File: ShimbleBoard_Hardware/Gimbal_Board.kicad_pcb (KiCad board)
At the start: 2 copper layers, 57 parts, among them Q1 2N3904, Q2 2N3904, Q3 2N3904, Q4 2N3904, Q5 2N3904, Q6 2N3904, Q7 2N3904, Q8 2N3904, U1 TM4C129E_Launchpad, U2 OKI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

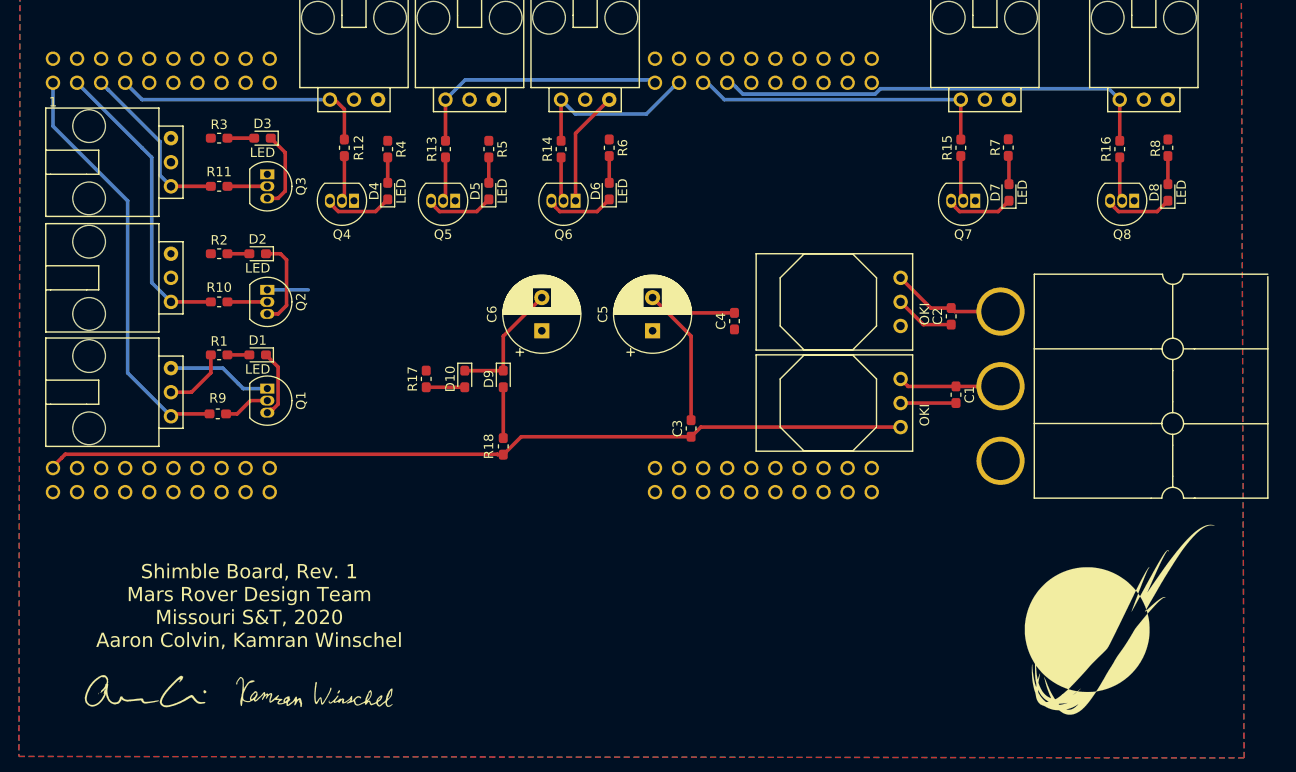
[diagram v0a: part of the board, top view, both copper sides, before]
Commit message: BJT changes
BJT changed to surface mount
Minor re-wiring
Ground & +5VA plains changed to solid
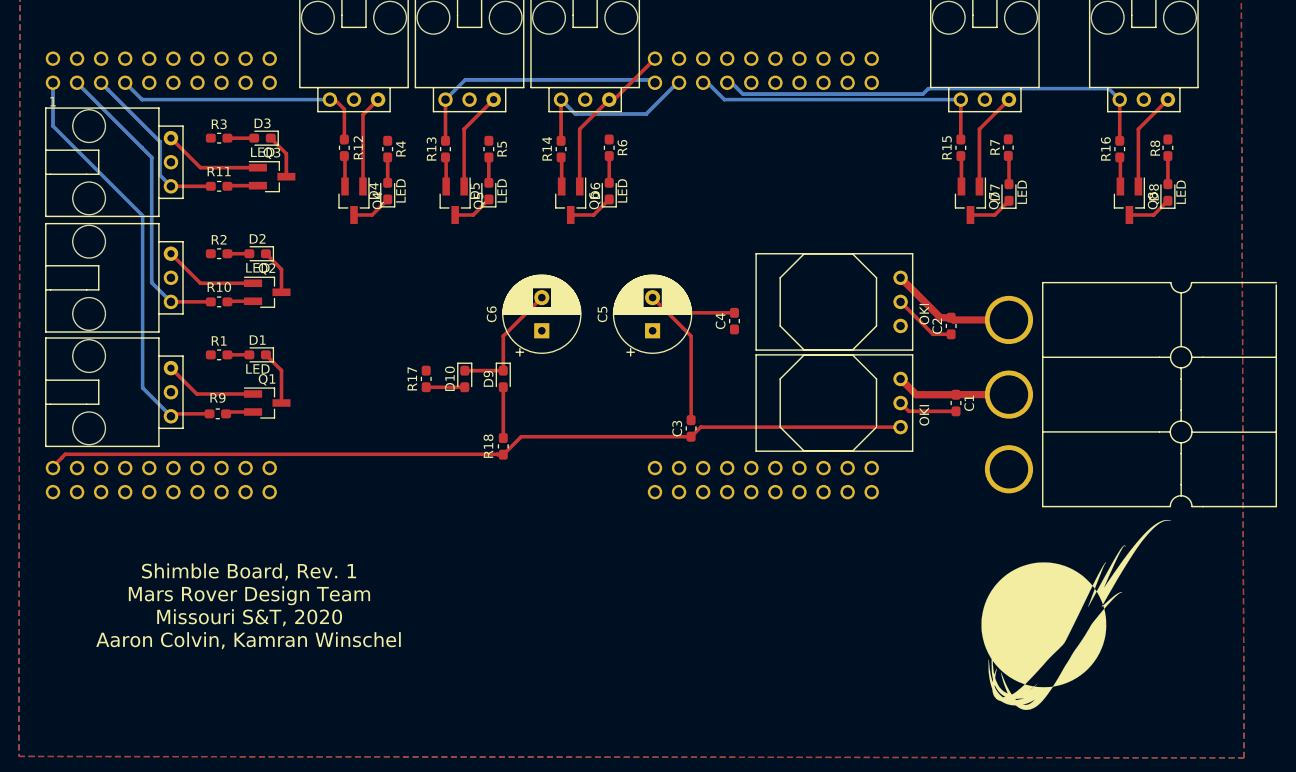
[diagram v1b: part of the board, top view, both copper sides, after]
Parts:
- removed the G*** at (97.0, 127.5)
- removed the G*** at (79.2, 127.5)
- Q1, Q2, Q3, Q4, Q5, Q6, Q7, Q8: footprint Package_TO_SOT_THT:TO-92_Inline -> Package_TO_SOT_SMD:SOT-23_Handsoldering
- moved G*** 4.60 mm to (177.3, 119.4)
- moved Q1 1.52 mm to (91.9, 97.0), turned to 0 degrees
- moved Conn9 1.26 mm to (173.7, 84.3)
- moved C2 1.02 mm to (164.1, 88.9)
- moved C1 0.88 mm to (164.6, 97.0)
- moved Q3 0.57 mm to (92.5, 73.2), turned to 0 degrees
- moved Q8 0.51 mm to (182.9, 75.7), turned to 270 degrees
- moved Q6 0.51 mm to (124.0, 75.7), turned to 270 degrees
- moved Q7 0.51 mm to (166.1, 75.7), turned to 270 degrees
- moved Q2 0.25 mm to (91.9, 85.3), turned to 0 degrees
- turned Q4 to 270 degrees
- turned Q5 to 270 degrees
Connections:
- U1 pad +5V: Net-(U1-Pad+5V) -> +5VL
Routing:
- net GND: track 74.8 -> 136.5 mm
- net +5VA: track 6.94 -> 0.00 mm
- net Net-(D2-Pad1): track 9.66 -> 4.74 mm
- net Net-(D3-Pad1): track 8.43 -> 4.74 mm
- net Net-(D5-Pad1): track 7.25 -> 4.24 mm
- net Net-(D4-Pad1): track 7.25 -> 4.24 mm
- net Net-(D7-Pad1): track 7.19 -> 4.69 mm
- net Net-(D6-Pad1): track 7.25 -> 4.74 mm
- net Net-(D8-Pad1): track 7.19 -> 4.69 mm
- net Net-(Q1-Pad2): track 5.28 -> 2.93 mm
- net Net-(Q7-Pad2): track 4.82 -> 3.24 mm
- net Net-(Q6-Pad2): track 4.68 -> 3.10 mm
- net Net-(Q5-Pad2): track 4.68 -> 3.10 mm
- net Net-(Q8-Pad2): track 4.68 -> 3.10 mm
- net Net-(Q4-Pad2): track 4.82 -> 3.24 mm
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
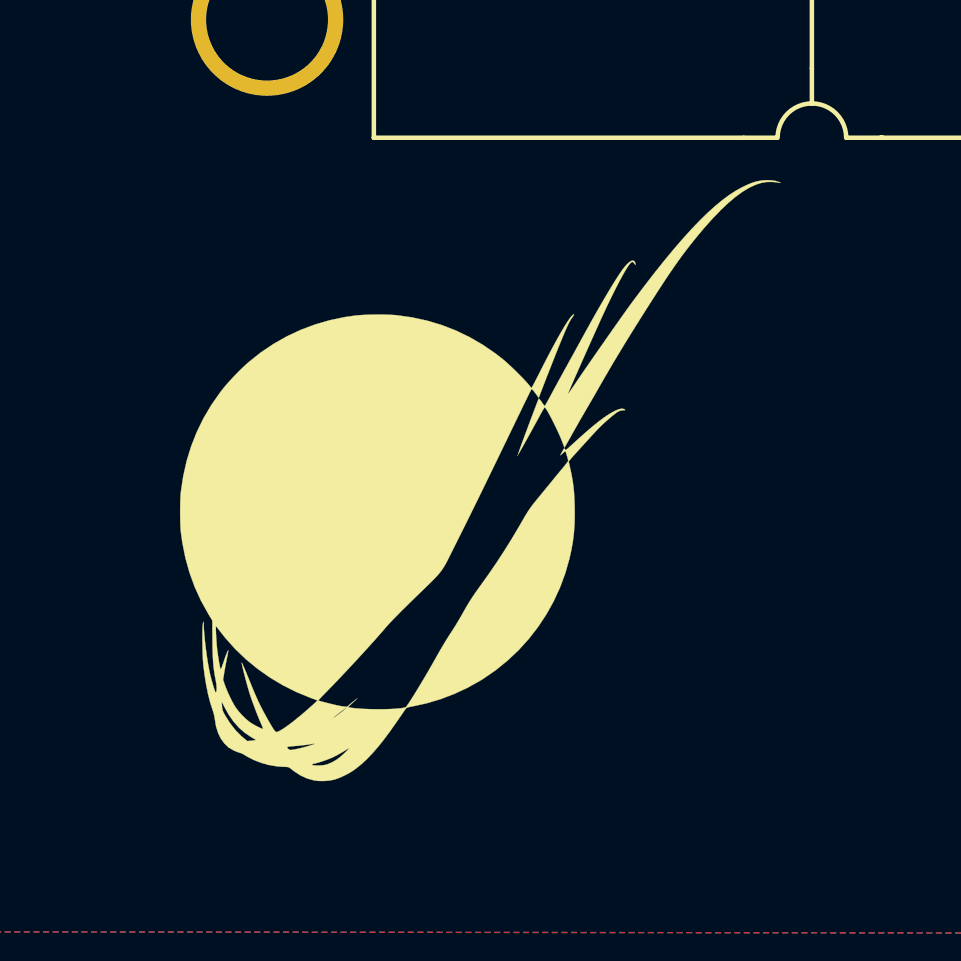
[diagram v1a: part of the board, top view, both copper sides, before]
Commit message: Resistor Changes
Resistors changed to 500 standard
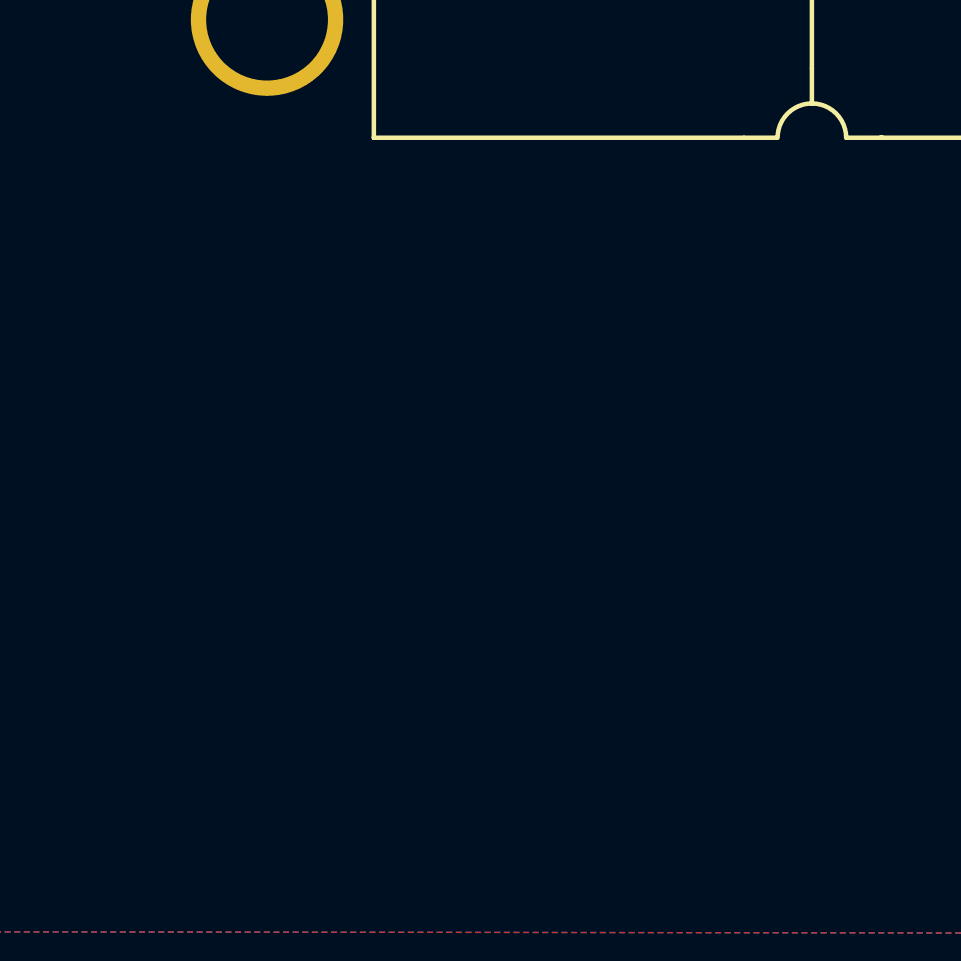
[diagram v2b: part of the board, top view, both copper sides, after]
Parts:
- removed G***: LOGO, MRDT_Silkscreens:0_MRDT_Logo_20mm
- R1, R10, R11, R12, R13, R14, R15, R16, R2, R3, R4, R5, R6, R7, R8, R9: value 100 -> 500
- R17, R18: value 1000 -> 500

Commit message: Major Overhaull
BJTs replaced by N-MOSFET
Buttons & switch added
PCB layout worked on (still not complete)
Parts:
- added D10: LED, Diode_SMD:D_0603_1608Metric_Pad1.05x0.95mm_HandSolder, F.Cu at (-66.5, 56.8)
- added D11: LED, Diode_SMD:D_0603_1608Metric_Pad1.05x0.95mm_HandSolder, F.Cu at (-56.9, 56.8)
- added D12: LED, Diode_SMD:D_0603_1608Metric_Pad1.05x0.95mm_HandSolder, F.Cu at (-47.2, 56.8)
- added D13: LED, Diode_SMD:D_0603_1608Metric_Pad1.05x0.95mm_HandSolder, F.Cu at (-83.3, 35.2)
- added D14: LED, Diode_SMD:D_0603_1608Metric_Pad1.05x0.95mm_HandSolder, F.Cu at (-73.7, 35.2)
- added D15: LED, Diode_SMD:D_0603_1608Metric_Pad1.05x0.95mm_HandSolder, F.Cu at (-64.0, 35.2)
- added D16: LED, Diode_SMD:D_0603_1608Metric_Pad1.05x0.95mm_HandSolder, F.Cu at (-54.4, 34.9)
- added D17: LED, Diode_SMD:D_0603_1608Metric_Pad1.05x0.95mm_HandSolder, F.Cu at (17.1, 49.8)
- added D18: LED, Diode_SMD:D_0603_1608Metric_Pad1.05x0.95mm_HandSolder, F.Cu at (46.2, 39.0)
- added D9: LED, Diode_SMD:D_0603_1608Metric_Pad1.05x0.95mm_HandSolder, F.Cu at (-76.2, 56.9)
- added R17: 500, Resistor_SMD:R_0603_1608Metric_Pad1.05x0.95mm_HandSolder, F.Cu at (-76.2, 53.3)
- added R18: 500, Resistor_SMD:R_0603_1608Metric_Pad1.05x0.95mm_HandSolder, F.Cu at (-66.5, 53.2)
- added R19: 500, Resistor_SMD:R_0603_1608Metric_Pad1.05x0.95mm_HandSolder, F.Cu at (-56.9, 53.2)
- added R20: 500, Resistor_SMD:R_0603_1608Metric_Pad1.05x0.95mm_HandSolder, F.Cu at (-47.2, 53.2)
- added R21: 500, Resistor_SMD:R_0603_1608Metric_Pad1.05x0.95mm_HandSolder, F.Cu at (-83.3, 38.7)
- added R22: 500, Resistor_SMD:R_0603_1608Metric_Pad1.05x0.95mm_HandSolder, F.Cu at (-73.7, 38.7)
- added R23: 500, Resistor_SMD:R_0603_1608Metric_Pad1.05x0.95mm_HandSolder, F.Cu at (-64.0, 38.7)
- added R24: 500, Resistor_SMD:R_0603_1608Metric_Pad1.05x0.95mm_HandSolder, F.Cu at (-54.4, 38.5)
- added R25: 500, Resistor_SMD:R_0603_1608Metric_Pad1.05x0.95mm_HandSolder, F.Cu at (20.7, 49.8)
- added R26: 500, Resistor_SMD:R_0603_1608Metric_Pad1.05x0.95mm_HandSolder, F.Cu at (46.2, 42.5)
- added SW1: SW_Push, Button_Switch_SMD:SW_SPST_TL3305A, F.Cu at (-79.8, 48.8)
- added SW10: SW_SPDT, Button_Switch_THT:SW_CuK_OS102011MA1QN1_SPDT_Angled, F.Cu at (42.2, 47.2)
- added SW2: SW_Push, Button_Switch_SMD:SW_SPST_TL3305A, F.Cu at (-70.1, 48.8)
- added SW3: SW_Push, Button_Switch_SMD:SW_SPST_TL3305A, F.Cu at (-60.5, 48.8)
- added SW4: SW_Push, Button_Switch_SMD:SW_SPST_TL3305A, F.Cu at (-50.8, 48.8)
- added SW5: SW_Push, Button_Switch_SMD:SW_SPST_TL3305A, F.Cu at (-79.8, 43.2)
- added SW6: SW_Push, Button_Switch_SMD:SW_SPST_TL3305A, F.Cu at (-70.1, 43.2)
- added SW7: SW_Push, Button_Switch_SMD:SW_SPST_TL3305A, F.Cu at (-60.5, 43.2)
- added SW8: SW_Push, Button_Switch_SMD:SW_SPST_TL3305A, F.Cu at (-50.8, 43.2)
- added SW9: SW_Push, Button_Switch_SMD:SW_SPST_TL3305A, F.Cu at (27.4, 48.3)
- Q1, Q2, Q3, Q4, Q5, Q6, Q7, Q8: value 2N3904 -> Q_NMOS_GDS
- moved D8 12.4 mm to (178.7, 65.5), turned to 180 degrees
- moved D7 10.2 mm to (166.0, 65.5), turned to 180 degrees
- moved R8 10.1 mm to (177.0, 68.2), turned to 90 degrees
- moved D4 9.39 mm to (102.5, 65.5), turned to 180 degrees
- moved D5 9.14 mm to (115.2, 65.5), turned to 180 degrees
- moved D6 9.14 mm to (127.9, 65.5), turned to 180 degrees
- moved D1 8.46 mm to (83.3, 95.6), turned to 270 degrees
- moved D3 8.21 mm to (83.3, 70.2), turned to 270 degrees
- moved Q6 8.16 mm to (128.8, 69.1), turned to 90 degrees
- moved Q5 7.87 mm to (116.1, 69.1), turned to 90 degrees
- moved D2 7.79 mm to (83.3, 82.9), turned to 270 degrees
- moved Q8 7.33 mm to (179.6, 69.1), turned to 90 degrees
- moved Q4 6.97 mm to (103.4, 69.1), turned to 90 degrees
- moved Conn8 6.78 mm to (177.8, 63.5)
- moved Q3 6.74 mm to (86.9, 69.3), turned to 180 degrees
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- renumbered D10 to D19, D9 to D20, R17 to R27, R18 to R28
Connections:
- Q1 pad 1: GND -> Net-(Q1-Pad1)
- Q1 pad 2: Net-(Q1-Pad2) -> GND
- Q2 pad 1: GND -> Net-(Q2-Pad1)
- Q2 pad 2: Net-(Q2-Pad2) -> GND
- Q3 pad 1: GND -> Net-(Q3-Pad1)
- Q3 pad 2: Net-(Q3-Pad2) -> GND
- Q4 pad 1: GND -> Net-(Q4-Pad1)
- Q4 pad 2: Net-(Q4-Pad2) -> GND
- Q5 pad 1: GND -> Net-(Q5-Pad1)
- Q5 pad 2: Net-(Q5-Pad2) -> GND
- Q6 pad 1: GND -> Net-(Q6-Pad1)
- Q6 pad 2: Net-(Q6-Pad2) -> GND
- Q7 pad 1: GND -> Net-(Q7-Pad1)
- Q7 pad 2: Net-(Q7-Pad2) -> GND
- Q8 pad 1: GND -> Net-(Q8-Pad1)
- Q8 pad 2: Net-(Q8-Pad2) -> GND
- R10 pad 1: Net-(Q2-Pad2) -> Net-(Q2-Pad1)
- R11 pad 1: Net-(Q3-Pad2) -> Net-(Q3-Pad1)
- R12 pad 1: Net-(Q4-Pad2) -> Net-(Q4-Pad1)
- R13 pad 1: Net-(Q5-Pad2) -> Net-(Q5-Pad1)
- R14 pad 1: Net-(Q6-Pad2) -> Net-(Q6-Pad1)
- R15 pad 1: Net-(Q7-Pad2) -> Net-(Q7-Pad1)
- R16 pad 1: Net-(Q8-Pad2) -> Net-(Q8-Pad1)
- R9 pad 1: Net-(Q1-Pad2) -> Net-(Q1-Pad1)
- U1 pad +3V3: Net-(U1-Pad+3V3) -> +3V3
- U1 pad PD2: Net-(U1-PadPD2) -> All_Servo_SW
- U1 pad PK1: Net-(U1-PadPK1) -> Servo_SW_7
- U1 pad PK2: Net-(U1-PadPK2) -> Servo_SW_8
- U1 pad PK3: Net-(U1-PadPK3) -> Servo_Setup_SW
- U1 pad PN4: Net-(U1-PadPN4) -> Servo_SW_6
- U1 pad PN5: Net-(U1-PadPN5) -> Servo_SW_5
- U1 pad PP0: Net-(U1-PadPP0) -> Servo_SW_1
- U1 pad PP1: Net-(U1-PadPP1) -> Servo_SW_2
- U1 pad PP4: Net-(U1-PadPP4) -> Servo_SW_4
- U1 pad PQ0: Net-(U1-PadPQ0) -> Servo_SW_3
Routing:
- net +5VL: track 91.0 -> 43.1 mm
- net GND: track 136.5 -> 105.6 mm
- net Servo_Ctrl_1: track 44.5 -> 48.3 mm
- net Servo_Ctrl_4: track 27.0 -> 30.7 mm
- net Net-(D1-Pad1): track 5.76 -> 2.08 mm
- net Net-(Q3-Pad2): track 3.24 -> 0.00 mm
- net Net-(Q7-Pad2): track 3.24 -> 0.00 mm
- net Net-(Q4-Pad2): track 3.24 -> 0.00 mm
- net Servo_Ctrl_2: track 31.4 -> 34.6 mm
- net Net-(Q8-Pad2): track 3.10 -> 0.00 mm
- net Net-(Q5-Pad2): track 3.10 -> 0.00 mm
- net Net-(Q6-Pad2): track 3.10 -> 0.00 mm
- net Servo_Ctrl_5: track 27.5 -> 30.5 mm
- net Net-(Q1-Pad2): track 2.93 -> 0.00 mm
- net Net-(Q2-Pad2): track 2.73 -> 0.00 mm
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
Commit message: PCB placement (not finished
PCB component placement and wiring
Still needs a lot more work, button pins need to be determined
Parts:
- moved D16 222.7 mm to (161.7, 89.2), turned to 180 degrees
- moved D15 222.2 mm to (151.5, 89.2), turned to 180 degrees
- moved D13 221.2 mm to (131.2, 89.2), turned to 180 degrees
- moved R24 218.7 mm to (158.4, 89.2), turned to 0 degrees
- moved D14 218.1 mm to (138.1, 87.6), turned to 0 degrees
- moved R23 218.1 mm to (148.2, 89.2), turned to 0 degrees
- moved R22 217.6 mm to (138.0, 89.2), turned to 0 degrees
- moved SW8 217.5 mm to (161.1, 92.5)
- moved SW4 217.4 mm to (161.1, 97.6)
- moved R21 217.1 mm to (127.9, 89.2), turned to 0 degrees
- moved SW7 217.0 mm to (150.9, 92.5)
- moved SW3 216.9 mm to (150.9, 97.6)
- moved SW6 216.6 mm to (140.8, 92.5)
- moved SW2 216.4 mm to (140.8, 97.6)
- moved SW5 216.1 mm to (130.6, 92.5)
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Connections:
- D17 pad 1: Net-(D17-Pad1) -> GND
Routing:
- net +3V3: track 0.00 -> 88.0 mm
- net GND: track 105.6 -> 70.3 mm, vias 0 -> 1
- net Servo_Ctrl_6: track 21.0 -> 55.7 mm
- net Servo_Ctrl_4: track 30.7 -> 57.3 mm
- net Servo_Ctrl_3: track 20.8 -> 47.2 mm
- net Servo_Ctrl_1: track 48.3 -> 23.0 mm
- net Servo_Ctrl_5: track 30.5 -> 46.4 mm
- net Servo_Ctrl_8: track 44.9 -> 29.8 mm
- net Servo_Ctrl_7: track 33.7 -> 48.4 mm
- net Servo_Setup_SW: track 0.00 -> 9.25 mm
- net Servo_SW_8: track 0.00 -> 9.03 mm
- net Servo_SW_7: track 0.00 -> 9.03 mm
- net Servo_SW_6: track 0.00 -> 9.03 mm
- net Servo_SW_5: track 0.00 -> 9.03 mm
- net Servo_SW_4: track 0.00 -> 8.98 mm
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
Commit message: Layout changes
Moved some stuff
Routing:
- net GND: track 70.3 -> 84.0 mm, vias 1 -> 2
- net Net-(D14-Pad2): track 0.00 -> 1.54 mm
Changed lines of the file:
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@@
     (thickness 1.6)
     (drawings 1)
-    (tracks 211)
+    (tracks 221)
     (zones 0)
     (modules 84)
@@
   (segment (start 180.086 73.914) (end 180.34 73.66) (width 0.381) (layer F.Cu) (net 2))
   (segment (start 173.228 73.914) (end 180.086 73.914) (width 0.381) (layer F.Cu) (net 2))
+  (segment (start 162.532 86.642) (end 163.068 86.106) (width 0.381) (layer F.Cu) (net 2))
+  (segment (start 162.532 89.154) (end 162.532 86.642) (width 0.381) (layer F.Cu) (net 2))
+  (segment (start 155.166 86.36) (end 155.956 86.36) (width 0.381) (layer F.Cu) (net 2))
+  (segment (start 152.372 89.154) (end 155.166 86.36) (width 0.381) (layer F.Cu) (net 2))
+  (segment (start 133.576 87.63) (end 132.052 89.154) (width 0.381) (layer F.Cu) (net 2))
+  (segment (start 137.188 87.63) (end 133.604 87.63) (width 0.381) (layer F.Cu) (net 2))
+  (segment (start 133.604 87.63) (end 133.576 87.63) (width 0.381) (layer F.Cu) (net 2))
+  (via (at 133.604 87.63) (size 0.8) (drill 0.4) (layers F.Cu B.Cu) (net 2))
   (segment (start 90.918 97.663) (end 90.932 97.649) (width 0.762) (layer F.Cu) (net 3))
   (segment (start 87.376 97.663) (end 90.918 97.663) (width 0.762) (layer F.Cu) (net 3))
@@
   (segment (start 159.23 100.838) (end 160.782 100.838) (width 0.381) (layer F.Cu) (net 86))
   (segment (start 128.75 89.154) (end 130.302 89.154) (width 0.381) (layer F.Cu) (net 87))
+  (segment (start 138.938 89.126) (end 138.91 89.154) (width 0.381) (layer F.Cu) (net 88))
+  (segment (start 138.938 87.63) (end 138.938 89.126) (width 0.381) (layer F.Cu) (net 88))
   (segment (start 149.07 89.154) (end 150.622 89.154) (width 0.381) (layer F.Cu) (net 89))
   (segment (start 160.782 89.154) (end 159.23 89.154) (width 0.381) (layer F.Cu) (net 90))

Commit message: Cleaned some stuff
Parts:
- added C7: 470u, Capacitor_THT:CP_Radial_D8.0mm_P3.50mm, F.Cu at (119.4, 81.3)
- moved C6 92.0 mm to (130.6, 81.0), turned to 90 degrees
- moved C5 69.1 mm to (142.2, 81.0), turned to 90 degrees
- moved C4 62.9 mm to (151.1, 79.6), turned to 90 degrees
- moved D16 45.2 mm to (116.4, 89.2)
- moved SW8 45.2 mm to (115.9, 92.5)
- moved R24 45.2 mm to (113.1, 89.2)
- moved D13 26.2 mm to (157.3, 89.2)
- moved R21 26.2 mm to (154.0, 89.2)
- moved SW5 26.2 mm to (156.8, 92.5)
- moved D15 21.6 mm to (129.9, 89.2)
- moved R23 21.6 mm to (126.6, 89.2)
- moved SW7 21.6 mm to (129.3, 92.5)
- moved D9 14.7 mm to (116.4, 100.8)
- moved R17 14.7 mm to (113.1, 100.8)
- moved SW1 14.7 mm to (115.9, 97.6)
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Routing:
- net +3V3: track 88.0 -> 147.4 mm, vias 0 -> 1
- net GND: track 84.0 -> 100.5 mm, vias 2 -> 1
- net Servo_Ctrl_5: track 46.4 -> 57.3 mm, vias 0 -> 1
- net +5VL: track 40.4 -> 47.7 mm
- net +5VA: track 0.00 -> 6.59 mm
- net All_Servo_SW: track 0.00 -> 6.36 mm
- net Servo_Ctrl_6: track 55.7 -> 50.1 mm, vias 0 -> 1
- net Servo_Ctrl_1: track 23.0 -> 27.4 mm, vias 0 -> 1
- net Servo_Ctrl_4: track 57.3 -> 54.2 mm
- net Servo_Ctrl_3: track 47.2 -> 45.5 mm
- net Net-(D18-Pad2): track 0.00 -> 1.55 mm
- net Servo_Ctrl_7: track 48.4 -> 49.2 mm, vias 0 -> 1
- net Servo_Ctrl_2: track 35.4 -> 34.8 mm
